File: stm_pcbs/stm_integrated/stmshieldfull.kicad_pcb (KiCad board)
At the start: 2 copper layers, 150 x 122 mm, 113 parts, among them P2 BNC, P5 BNC, P6 CONN_20X2, U11 AD5791, U13 AD8676, U14 AD8675, U15 A9_REFERENCE, U16 LT1019ACS8, U17 LTC1859, U2 AD5791, U4 AD8676, U5 AD5791, U6 AD8675, U8 AD5791

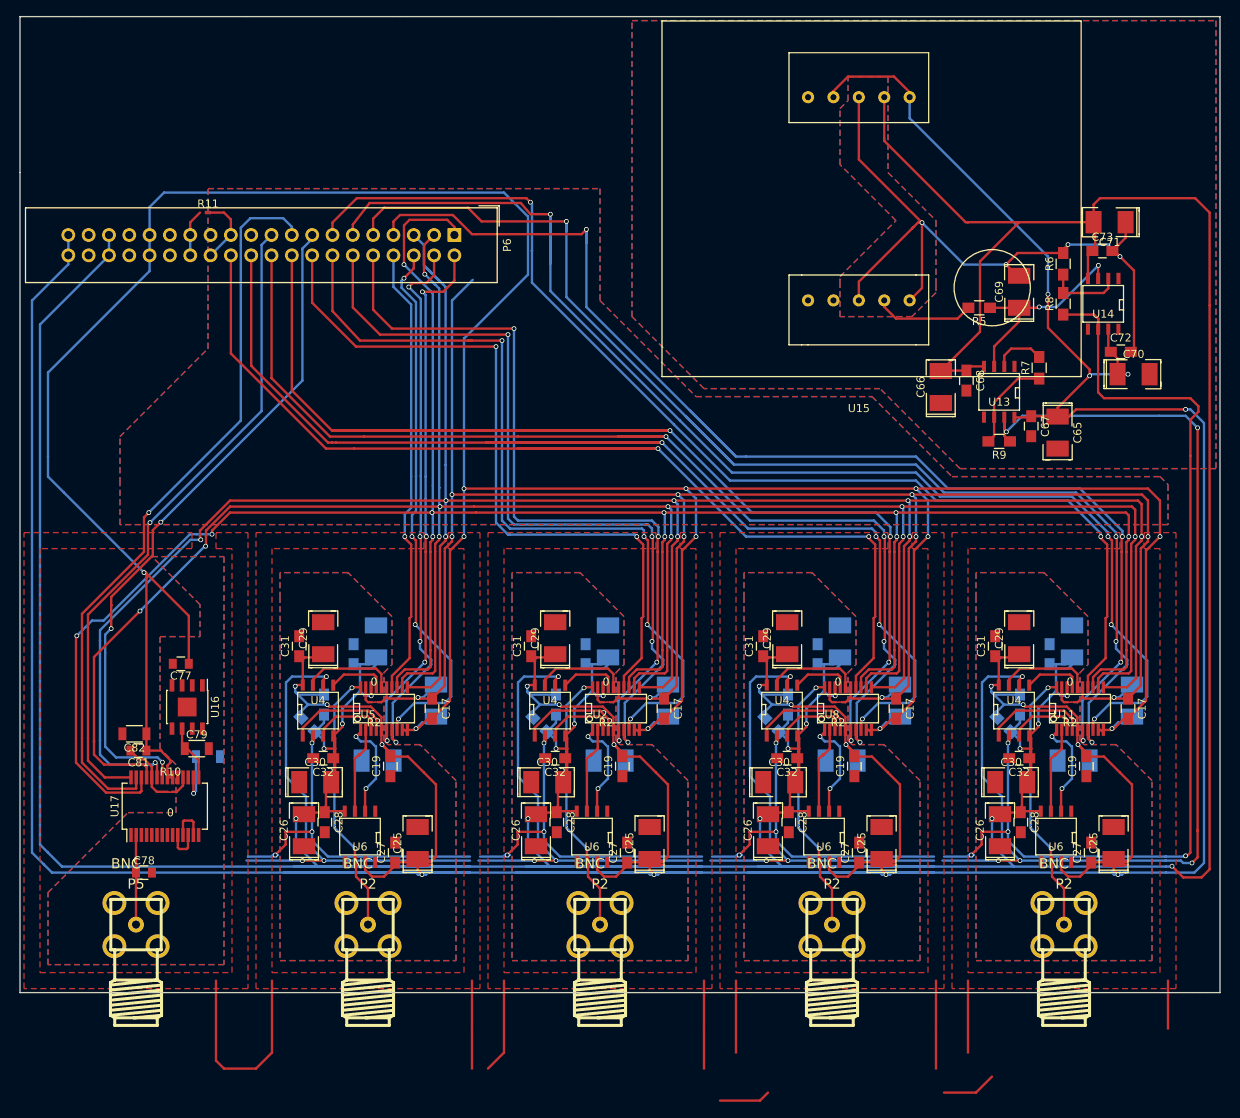
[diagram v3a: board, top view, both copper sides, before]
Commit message: fixed issue with DAC (opamp wiring was wrong)
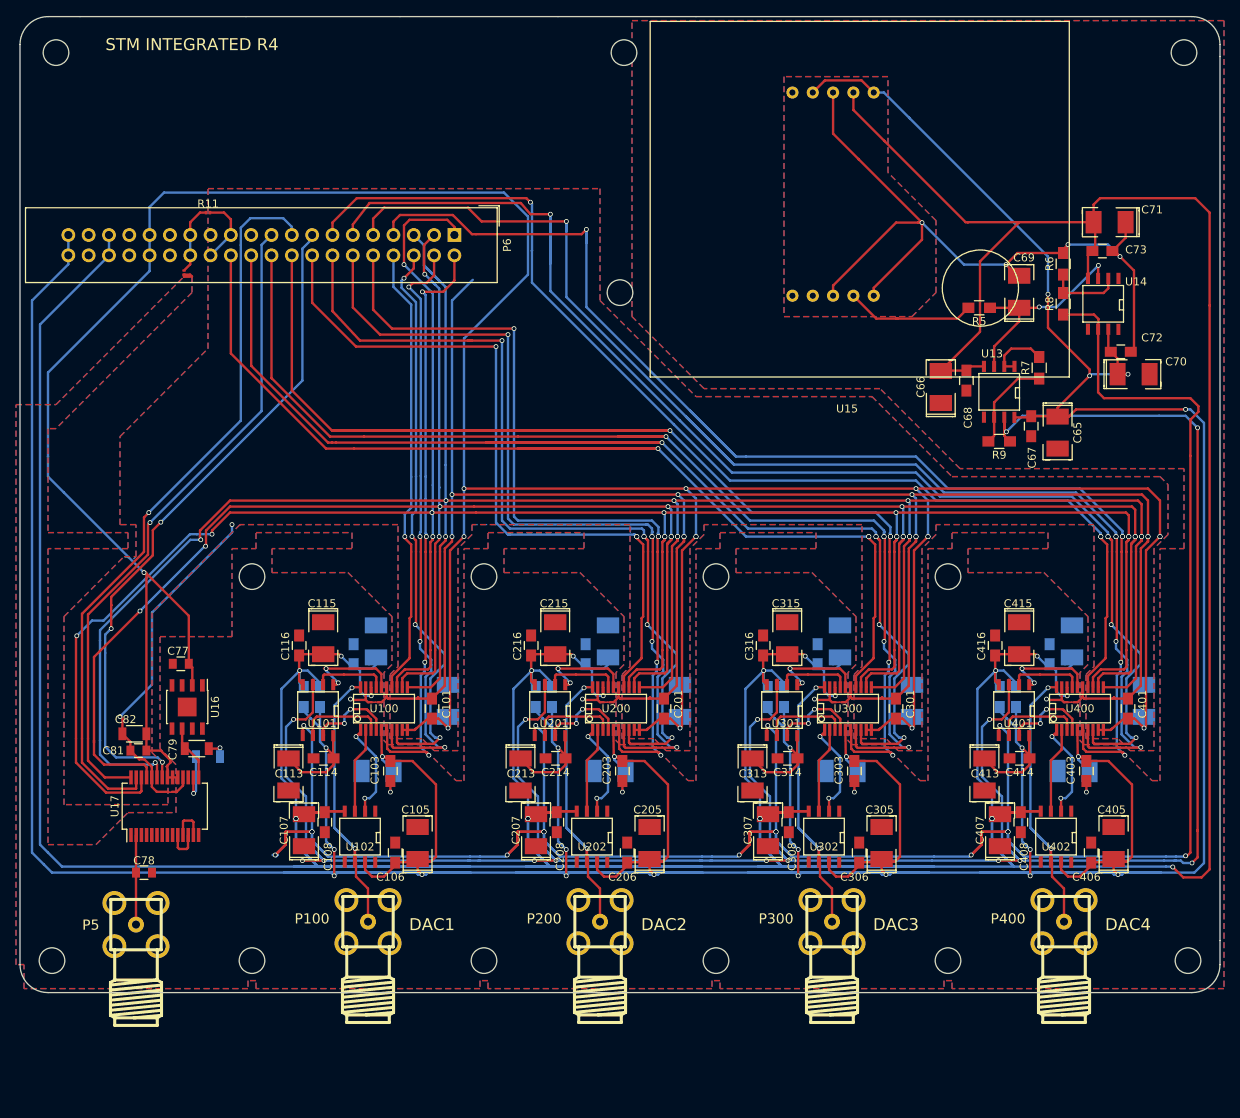
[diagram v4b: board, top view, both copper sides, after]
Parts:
- removed C17 (x4), C19 (x4), C21 (x4), C23 (x4), C24 (x4), C27 (x3), C28 (x4), C31 (x4), C32 (x4): 0.1uF, Capacitors_SMD:C_0805_HandSoldering
- removed C18 (x4), C20 (x4), C22 (x4), C25 (x3), C26 (x3), C29 (x4), C30 (x4): 10uF, stm:SMD-1210_Pol
- removed P2 (x3): BNC, stm:SMA
- removed R2 (x4): 0, stm:0Ohm
- removed U11, U2, U5, U8: AD5791, stm:SSOP-20
- removed U4 (x4): AD8676, stm:SOIC-8
- removed U6 (x3): AD8675, stm:SOIC-8
- added C101: 0.1uF, Capacitors_SMD:C_0805_HandSoldering, F.Cu at (125.0, 123.4)
- added C102: 10uF, stm:SMD-1210_Pol, B.Cu at (127.0, 122.4)
- added C103: 0.1uF, Capacitors_SMD:C_0805_HandSoldering, F.Cu at (119.8, 131.2)
- added C104: 10uF, stm:SMD-1210_Pol, B.Cu at (118.2, 131.2)
- added C108: 0.1uF, Capacitors_SMD:C_0805_HandSoldering, F.Cu at (111.6, 137.6)
- added C109: 0.1uF, Capacitors_SMD:C_0805_HandSoldering, B.Cu at (115.2, 116.6)
- added C110: 10uF, stm:SMD-1210_Pol, B.Cu at (118.0, 115.0)
- added C111: 0.1uF, Capacitors_SMD:C_0805_HandSoldering, B.Cu at (109.0, 121.9)
- added C112: 0.1uF, Capacitors_SMD:C_0805_HandSoldering, B.Cu at (111.0, 121.9)
- added C113: 10uF, stm:SMD-1210_Pol, F.Cu at (107.1, 131.6)
- added C114: 0.1uF, Capacitors_SMD:C_0805_HandSoldering, F.Cu at (111.4, 129.6)
- added C115: 10uF, stm:SMD-1210_Pol, F.Cu at (111.4, 114.6)
- added C116: 0.1uF, Capacitors_SMD:C_0805_HandSoldering, F.Cu at (108.4, 115.5)
- added C201: 0.1uF, Capacitors_SMD:C_0805_HandSoldering, F.Cu at (154.0, 123.4)
- added C202: 10uF, stm:SMD-1210_Pol, B.Cu at (156.0, 122.4)
- added C203: 0.1uF, Capacitors_SMD:C_0805_HandSoldering, F.Cu at (148.8, 131.2)
- added C204: 10uF, stm:SMD-1210_Pol, B.Cu at (147.2, 131.2)
- added C205: 10uF, stm:SMD-1210_Pol, F.Cu at (152.2, 140.2)
- added C206: 0.1uF, Capacitors_SMD:C_0805_HandSoldering, F.Cu at (149.4, 141.4)
- added C207: 10uF, stm:SMD-1210_Pol, F.Cu at (138.0, 138.6)
- added C208: 0.1uF, Capacitors_SMD:C_0805_HandSoldering, F.Cu at (140.6, 137.6)
- added C209: 0.1uF, Capacitors_SMD:C_0805_HandSoldering, B.Cu at (144.2, 116.6)
- added C210: 10uF, stm:SMD-1210_Pol, B.Cu at (147.0, 115.0)
- added C211: 0.1uF, Capacitors_SMD:C_0805_HandSoldering, B.Cu at (138.0, 121.9)
- added C212: 0.1uF, Capacitors_SMD:C_0805_HandSoldering, B.Cu at (140.0, 121.9)
- added C213: 10uF, stm:SMD-1210_Pol, F.Cu at (136.1, 131.6)
- added C214: 0.1uF, Capacitors_SMD:C_0805_HandSoldering, F.Cu at (140.4, 129.6)
- added C215: 10uF, stm:SMD-1210_Pol, F.Cu at (140.4, 114.6)
- added C216: 0.1uF, Capacitors_SMD:C_0805_HandSoldering, F.Cu at (137.4, 115.5)
- added C301: 0.1uF, Capacitors_SMD:C_0805_HandSoldering, F.Cu at (183.0, 123.4)
- added C302: 10uF, stm:SMD-1210_Pol, B.Cu at (185.0, 122.4)
- added C303: 0.1uF, Capacitors_SMD:C_0805_HandSoldering, F.Cu at (177.8, 131.2)
- added C304: 10uF, stm:SMD-1210_Pol, B.Cu at (176.2, 131.2)
- added C305: 10uF, stm:SMD-1210_Pol, F.Cu at (181.2, 140.2)
- added C306: 0.1uF, Capacitors_SMD:C_0805_HandSoldering, F.Cu at (178.4, 141.4)
- added C307: 10uF, stm:SMD-1210_Pol, F.Cu at (167.0, 138.6)
- added C308: 0.1uF, Capacitors_SMD:C_0805_HandSoldering, F.Cu at (169.6, 137.6)
- added C309: 0.1uF, Capacitors_SMD:C_0805_HandSoldering, B.Cu at (173.2, 116.6)
- added C310: 10uF, stm:SMD-1210_Pol, B.Cu at (176.0, 115.0)
- added C311: 0.1uF, Capacitors_SMD:C_0805_HandSoldering, B.Cu at (167.0, 121.9)
- added C312: 0.1uF, Capacitors_SMD:C_0805_HandSoldering, B.Cu at (169.0, 121.9)
- added C313: 10uF, stm:SMD-1210_Pol, F.Cu at (165.1, 131.6)
- added C314: 0.1uF, Capacitors_SMD:C_0805_HandSoldering, F.Cu at (169.4, 129.6)
- added C315: 10uF, stm:SMD-1210_Pol, F.Cu at (169.4, 114.6)
- added C316: 0.1uF, Capacitors_SMD:C_0805_HandSoldering, F.Cu at (166.4, 115.5)
- added C401: 0.1uF, Capacitors_SMD:C_0805_HandSoldering, F.Cu at (212.0, 123.4)
- added C402: 10uF, stm:SMD-1210_Pol, B.Cu at (214.0, 122.4)
- added C403: 0.1uF, Capacitors_SMD:C_0805_HandSoldering, F.Cu at (206.8, 131.2)
- added C404: 10uF, stm:SMD-1210_Pol, B.Cu at (205.2, 131.2)
- added C405: 10uF, stm:SMD-1210_Pol, F.Cu at (210.2, 140.2)
- added C406: 0.1uF, Capacitors_SMD:C_0805_HandSoldering, F.Cu at (207.4, 141.4)
- added C407: 10uF, stm:SMD-1210_Pol, F.Cu at (196.0, 138.6)
- added C408: 0.1uF, Capacitors_SMD:C_0805_HandSoldering, F.Cu at (198.6, 137.6)
- added C409: 0.1uF, Capacitors_SMD:C_0805_HandSoldering, B.Cu at (202.2, 116.6)
- added C410: 10uF, stm:SMD-1210_Pol, B.Cu at (205.0, 115.0)
- added C411: 0.1uF, Capacitors_SMD:C_0805_HandSoldering, B.Cu at (196.0, 121.9)
- added C412: 0.1uF, Capacitors_SMD:C_0805_HandSoldering, B.Cu at (198.0, 121.9)
- added C413: 10uF, stm:SMD-1210_Pol, F.Cu at (194.1, 131.6)
- added C414: 0.1uF, Capacitors_SMD:C_0805_HandSoldering, F.Cu at (198.4, 129.6)
- added C415: 10uF, stm:SMD-1210_Pol, F.Cu at (198.4, 114.6)
- added C416: 0.1uF, Capacitors_SMD:C_0805_HandSoldering, F.Cu at (195.4, 115.5)
- added P200: BNC, stm:SMA, F.Cu at (146.0, 150.0)
- added P300: BNC, stm:SMA, F.Cu at (175.0, 150.0)
- added P400: BNC, stm:SMA, F.Cu at (204.0, 150.0)
- added R100: 0, stm:0Ohm, F.Cu at (117.7, 122.6)
- added R12: 0, Resistors_SMD:R_0201_NoSilk, F.Cu at (94.0, 68.9)
- added R200: 0, stm:0Ohm, F.Cu at (146.7, 122.6)
- added R300: 0, stm:0Ohm, F.Cu at (175.7, 122.6)
- added R400: 0, stm:0Ohm, F.Cu at (204.7, 122.6)
- added REF**: MountingHole_3.2mm_M3, Mounting_Holes:MountingHole_3.2mm_M3, F.Cu at (189.5, 154.9)
- added REF**: MountingHole_3.2mm_M3, Mounting_Holes:MountingHole_3.2mm_M3, F.Cu at (219.0, 41.4)
- added REF**: MountingHole_3.2mm_M3, Mounting_Holes:MountingHole_3.2mm_M3, F.Cu at (102.5, 106.9)
- added REF**: MountingHole_3.2mm_M3, Mounting_Holes:MountingHole_3.2mm_M3, F.Cu at (102.5, 154.9)
- added REF**: MountingHole_3.2mm_M3, Mounting_Holes:MountingHole_3.2mm_M3, F.Cu at (131.5, 154.9)
- added REF**: MountingHole_3.2mm_M3, Mounting_Holes:MountingHole_3.2mm_M3, F.Cu at (131.5, 106.9)
- added REF**: MountingHole_3.2mm_M3, Mounting_Holes:MountingHole_3.2mm_M3, F.Cu at (189.5, 106.9)
- added REF**: MountingHole_3.2mm_M3, Mounting_Holes:MountingHole_3.2mm_M3, F.Cu at (160.5, 106.9)
- added REF**: MountingHole_3.2mm_M3, Mounting_Holes:MountingHole_3.2mm_M3, F.Cu at (160.5, 154.9)
- added REF**: MountingHole_3.2mm_M3, Mounting_Holes:MountingHole_3.2mm_M3, F.Cu at (77.5, 154.9)
- added REF**: MountingHole_3.2mm_M3, Mounting_Holes:MountingHole_3.2mm_M3, F.Cu at (219.5, 154.9)
- added REF**: MountingHole_3.2mm_M3, Mounting_Holes:MountingHole_3.2mm_M3, F.Cu at (148.5, 71.4)
- added REF**: MountingHole_3.2mm_M3, Mounting_Holes:MountingHole_3.2mm_M3, F.Cu at (149.0, 41.4)
- added REF**: MountingHole_3.2mm_M3, Mounting_Holes:MountingHole_3.2mm_M3, F.Cu at (78.0, 41.4)
- added U100: AD5791, stm:SSOP-20, F.Cu at (119.0, 123.4)
- added U101: AD8676, stm:SOIC-8, F.Cu at (110.8, 123.5)
- added U200: AD5791, stm:SSOP-20, F.Cu at (148.0, 123.4)
- added U201: AD8676, stm:SOIC-8, F.Cu at (139.8, 123.5)
- added U202: AD8675, stm:SOIC-8, F.Cu at (145.0, 139.4)
- added U300: AD5791, stm:SSOP-20, F.Cu at (177.0, 123.4)
- added U301: AD8676, stm:SOIC-8, F.Cu at (168.8, 123.5)
- added U302: AD8675, stm:SOIC-8, F.Cu at (174.0, 139.4)
- added U400: AD5791, stm:SSOP-20, F.Cu at (206.0, 123.4)
- added U401: AD8676, stm:SOIC-8, F.Cu at (197.8, 123.5)
- added U402: AD8675, stm:SOIC-8, F.Cu at (203.0, 139.4)
- moved U15 1.48 mm to (152.3, 81.9)
- moved P100 0.37 mm to (117.0, 150.0)
- renumbered C25 to C105, C27 to C106, C26 to C107, P2 to P100, U6 to U102
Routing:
- net +14V: track 739.3 -> 875.8 mm, vias 20 -> 24
- net -14V: track 683.0 -> 810.1 mm, vias 17 -> 21
- net (no net): track 109.3 -> 0.00 mm
- net Net-(P100-Pad1): track 133.5 -> 38.8 mm, vias 8 -> 2
- net Net-(U4-Pad1): track 51.7 -> 0.00 mm
- net +10VREF: track 267.2 -> 318.5 mm, vias 13 -> 17
- net Net-(U4-Pad7): track 47.0 -> 0.00 mm
- net Net-(P300-Pad1): track 0.00 -> 38.8 mm, vias 0 -> 2
- net Net-(P400-Pad1): track 0.00 -> 38.8 mm, vias 0 -> 2
- net Net-(P200-Pad1): track 0.00 -> 38.8 mm, vias 0 -> 2
- net Net-(U100-Pad1): track 51.0 -> 12.5 mm, vias 8 -> 2
- net Net-(U4-Pad3): track 35.7 -> 0.00 mm
- net Net-(U100-Pad2): track 44.1 -> 10.7 mm
- net Net-(U4-Pad5): track 29.4 -> 0.00 mm
- net AGND: track 104.6 -> 130.8 mm, vias 4 -> 13
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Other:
- outline, holes or cut-outs redrawn
- board text added: "DAC1"
- board text added: "DAC2"
- board text added: "DAC3"
- board text added: "DAC4"
- board text added: "STM INTEGRATED R4"

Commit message: update stm integrated design based on bring up...
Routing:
- net AGND: track 130.8 -> 126.0 mm
- net -14V: track 810.1 -> 807.9 mm
- net 7VREF: track 16.3 -> 18.2 mm
- net +14V: track 875.8 -> 876.7 mm
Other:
- board text added: "STM INTEGRATED R4a"
- board text removed: "STM INTEGRATED R4"

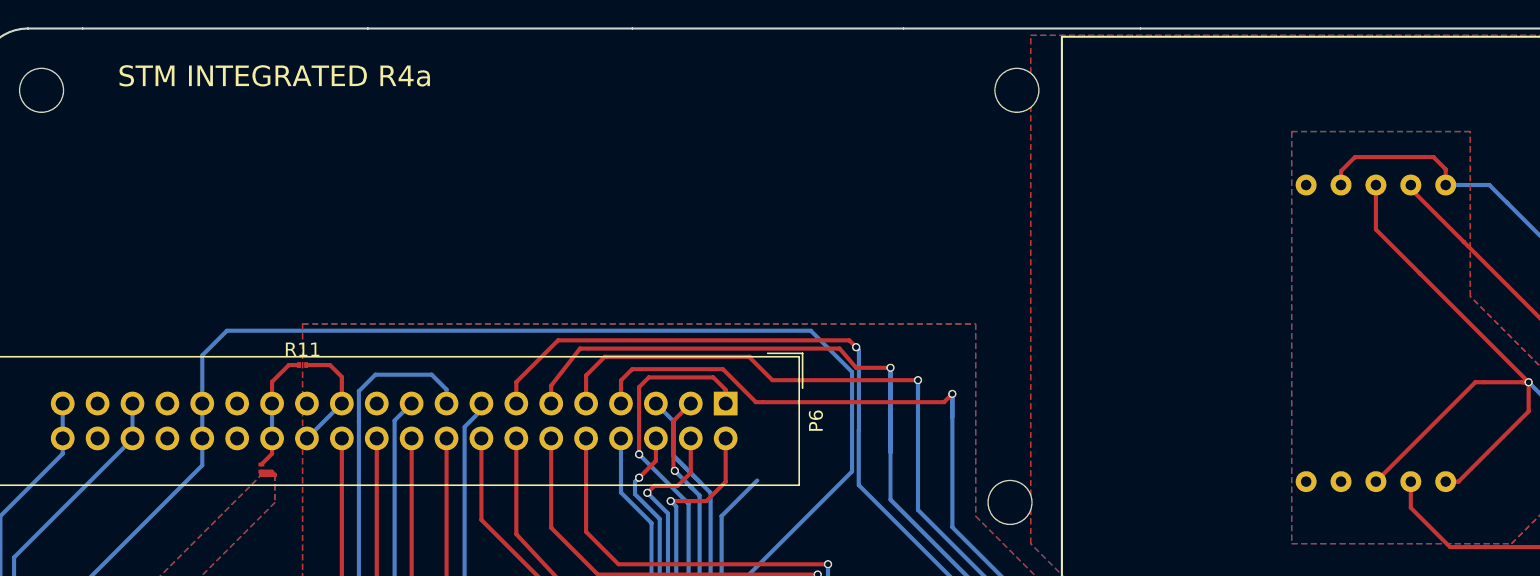
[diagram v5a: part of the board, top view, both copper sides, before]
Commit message: Trying FETs, two opamps in integrator
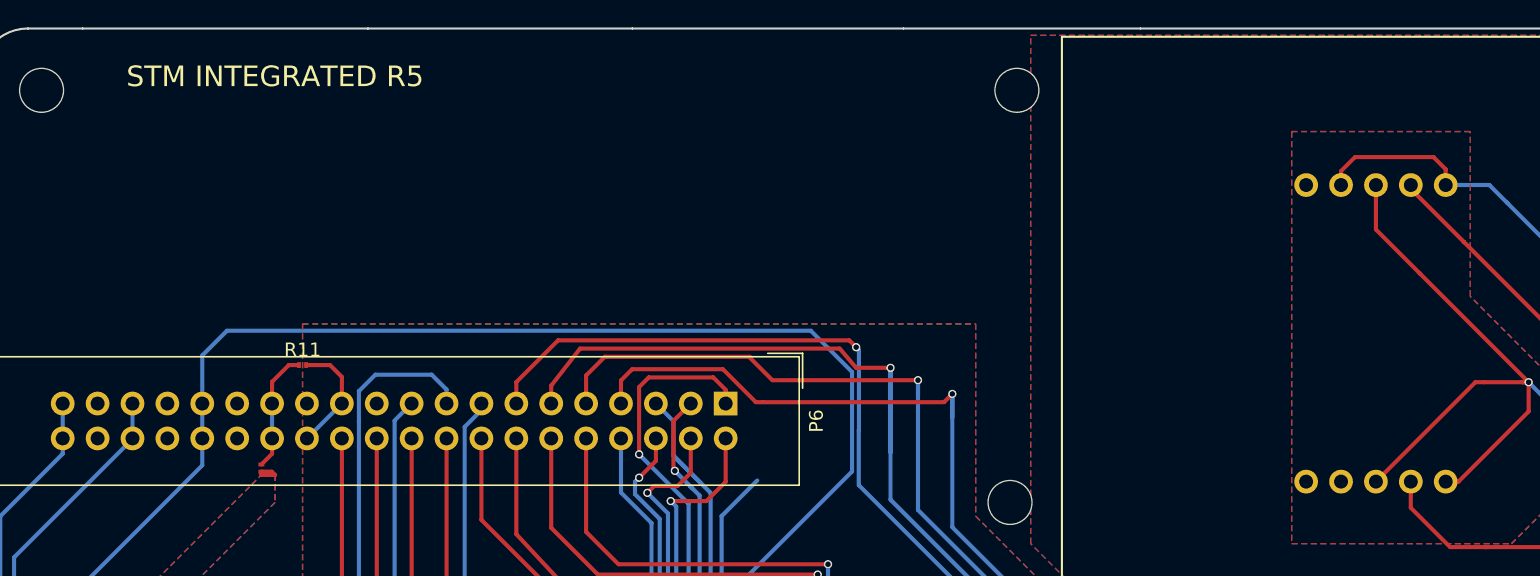
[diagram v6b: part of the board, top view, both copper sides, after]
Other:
- board text added: "STM INTEGRATED R5"
- board text removed: "STM INTEGRATED R4a"
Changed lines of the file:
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@@
     (fp_line (start 0 -44.45) (end 52.3875 -44.45) (layer F.SilkS) (width 0.15))
     (fp_line (start 52.3875 -44.45) (end 52.3875 0) (layer F.SilkS) (width 0.15))
-    (pad A1 thru_hole circle (at 17.78 -12.065) (size 1.524 1.524) (drill 0.762) (layers *.Cu *.Mask)
+    (pad A1 thru_hole circle (at 17.78 -12.065) (size 1.7272 1.7272) (drill 1.016) (layers *.Cu *.Mask)
       (net 61 "Net-(U15-PadA1)"))
-    (pad NC thru_hole circle (at 20.32 -12.065) (size 1.524 1.524) (drill 0.762) (layers *.Cu *.Mask))
-    (pad A2 thru_hole circle (at 22.86 -12.065) (size 1.524 1.524) (drill 0.762) (layers *.Cu *.Mask)
+    (pad NC thru_hole circle (at 20.32 -12.065) (size 1.7272 1.7272) (drill 1.016) (layers *.Cu *.Mask))
+    (pad A2 thru_hole circle (at 22.86 -12.065) (size 1.7272 1.7272) (drill 1.016) (layers *.Cu *.Mask)
       (net 1 AGND))
-    (pad A3 thru_hole circle (at 25.4 -12.065) (size 1.524 1.524) (drill 0.762) (layers *.Cu *.Mask)
+    (pad A3 thru_hole circle (at 25.4 -12.065) (size 1.7272 1.7272) (drill 1.016) (layers *.Cu *.Mask)
       (net 59 7VREF))
-    (pad A4 thru_hole circle (at 27.94 -12.065) (size 1.524 1.524) (drill 0.762) (layers *.Cu *.Mask)
+    (pad A4 thru_hole circle (at 27.94 -12.065) (size 1.7272 1.7272) (drill 1.016) (layers *.Cu *.Mask)
       (net 1 AGND))
-    (pad B2 thru_hole circle (at 20.32 -33.655) (size 1.524 1.524) (drill 0.762) (layers *.Cu *.Mask)
+    (pad B2 thru_hole circle (at 20.32 -33.655) (size 1.7272 1.7272) (drill 1.016) (layers *.Cu *.Mask)
       (net 4 +14V))
-    (pad B3 thru_hole circle (at 22.86 -33.655) (size 1.524 1.524) (drill 0.762) (layers *.Cu *.Mask)
+    (pad B3 thru_hole circle (at 22.86 -33.655) (size 1.7272 1.7272) (drill 1.016) (layers *.Cu *.Mask)
       (net 1 AGND))
-    (pad B1 thru_hole circle (at 17.78 -33.655) (size 1.524 1.524) (drill 0.762) (layers *.Cu *.Mask)
+    (pad B1 thru_hole circle (at 17.78 -33.655) (size 1.7272 1.7272) (drill 1.016) (layers *.Cu *.Mask)
       (net 60 "Net-(U15-PadB1)"))
-    (pad B4 thru_hole circle (at 25.4 -33.655) (size 1.524 1.524) (drill 0.762) (layers *.Cu *.Mask)
+    (pad B4 thru_hole circle (at 25.4 -33.655) (size 1.7272 1.7272) (drill 1.016) (layers *.Cu *.Mask)
       (net 5 -14V))
-    (pad B5 thru_hole circle (at 27.94 -33.655) (size 1.524 1.524) (drill 0.762) (layers *.Cu *.Mask)
+    (pad B5 thru_hole circle (at 27.94 -33.655) (size 1.7272 1.7272) (drill 1.016) (layers *.Cu *.Mask)
       (net 4 +14V))
   )
@@
     (effects (font (size 1.5 1.5) (thickness 0.3)))
   )
-  (gr_text "STM INTEGRATED R4a" (at 94.998 40.365) (layer F.SilkS)
+  (gr_text "STM INTEGRATED R5" (at 94.998 40.365) (layer F.SilkS)
     (effects (font (size 1.5 1.5) (thickness 0.3)))
   )
